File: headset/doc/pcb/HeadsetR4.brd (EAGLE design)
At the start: 85 x 56 mm, 58 parts, among them U1 STM32F405RGT6, U2 MAX17043, U3 MCP73831, U4 MIC5219, U5 MIC5219, U6 MIC5219 3.3V, U7 XBEE, U8 STEVAL-MKI108V2, Y1 8MHz

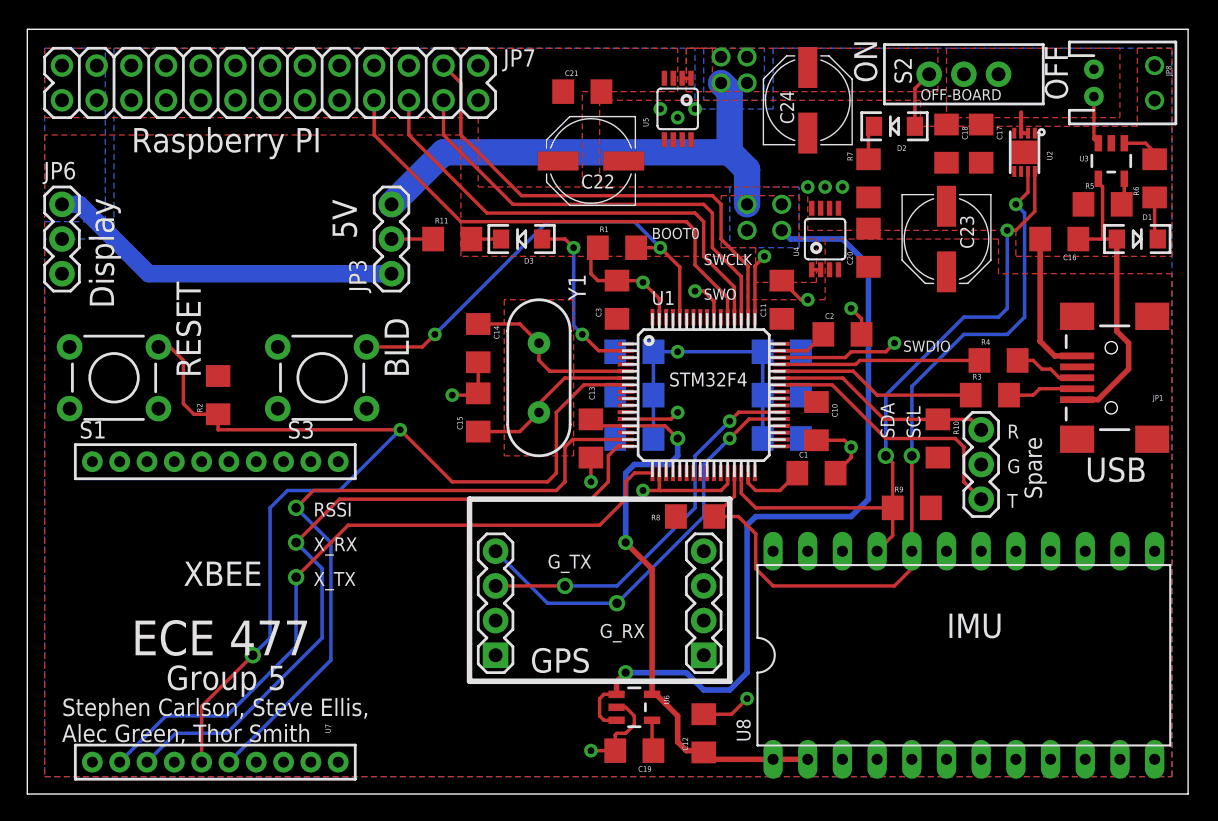
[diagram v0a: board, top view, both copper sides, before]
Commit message: Carlson updated pcb to add clearance on power planes.
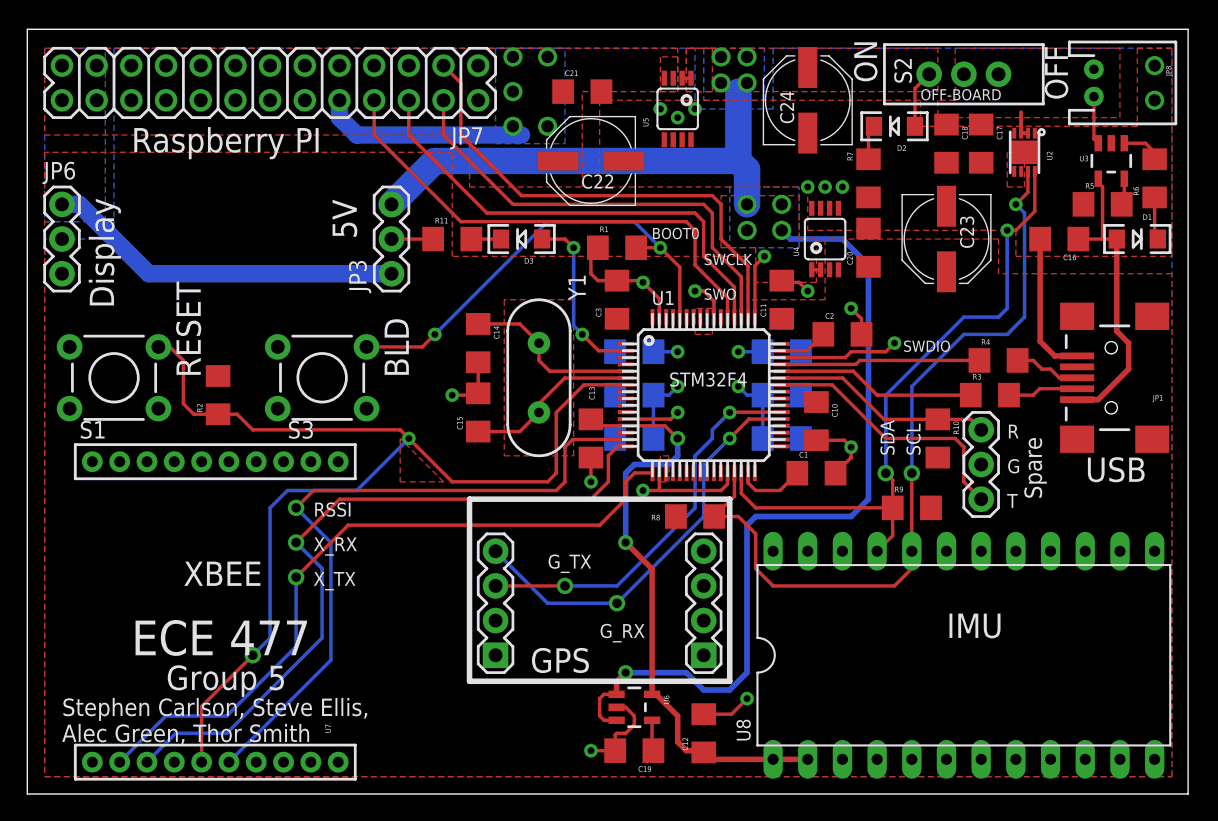
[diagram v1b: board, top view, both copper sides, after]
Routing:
- net V_CORE: track 0.00 -> 15.1 mm, vias 0 -> 5
- net V_MCU: track 20.7 -> 14.2 mm, vias 1 -> 4
- net V_IN: track 102.4 -> 101.6 mm
- added copper zone on layer 16, net V_CORE

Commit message: Carlson touched up pcb and schematic
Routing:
- net BC_STAT: track 3.01 -> 4.05 mm
- net X_RX: track 52.5 -> 52.0 mm
- net GND: vias 18 -> 20
- net BOOT0: vias 2 -> 1
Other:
- board text added: "!CS!"
- board text added: "5"
- board text added: "CHARGING"
- board text added: "GND"
- board text added: "MISO"
- board text added: "MOSI"
- board text added: "SCK"
- board text added: "STAT"
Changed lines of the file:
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@@
 <text x="2.54" y="3.81" size="1.27" layer="21">Stephen Carlson, Steve Ellis,
 Alec Green, Thor Smith</text>
-<text x="7.62" y="46.99" size="1.778" layer="21">Raspberry PI</text>
-<text x="6.35" y="35.56" size="1.778" layer="21" rot="R90">Display</text>
+<text x="5.715" y="46.99" size="1.778" layer="21">Raspberry PI</text>
+<text x="8.255" y="35.56" size="1.778" layer="21" rot="R90">Display</text>
 <text x="24.13" y="40.64" size="1.778" layer="21" rot="R90">5V</text>
 <text x="12.7" y="30.48" size="1.778" layer="21" rot="R90">RESET</text>
@@
 <text x="45.72" y="40.64" size="0.8128" layer="21">BOOT0</text>
 <text x="65.405" y="50.8" size="0.8128" layer="21">OFF-BOARD</text>
+<text x="18.415" y="20.32" size="1.016" layer="22" rot="MR0">RSSI</text>
+<text x="18.415" y="17.78" size="1.016" layer="22" rot="MR0">X_RX</text>
+<text x="18.415" y="15.24" size="1.016" layer="22" rot="MR0">X_TX</text>
+<text x="22.86" y="12.7" size="1.778" layer="22" rot="MR0">XBEE</text>
+<text x="40.64" y="12.7" size="1.016" layer="22" rot="MR0">G_TX</text>
+<text x="45.72" y="15.24" size="1.016" layer="22" rot="MR0">G_RX</text>
+<text x="71.12" y="11.43" size="1.778" layer="22" rot="MR0">IMU</text>
+<text x="78.74" y="29.21" size="1.778" layer="22" rot="MR0">USB</text>
+<text x="67.945" y="32.385" size="0.8128" layer="22" rot="MR0">SWDIO</text>
+<text x="53.34" y="38.735" size="0.8128" layer="22" rot="MR0">SWCLK</text>
+<text x="52.07" y="36.195" size="0.8128" layer="22" rot="MR0">SWO</text>
+<text x="49.53" y="40.64" size="0.8128" layer="22" rot="MR0">BOOT0</text>
+<text x="23.495" y="46.99" size="1.778" layer="22" rot="MR0">Raspberry PI</text>
+<text x="6.35" y="35.56" size="1.778" layer="22" rot="MR90">Display</text>
+<text x="22.86" y="40.64" size="1.778" layer="22" rot="MR90">5V</text>
+<text x="11.43" y="30.48" size="1.778" layer="22" rot="MR90">RESET</text>
+<text x="26.67" y="30.48" size="1.778" layer="22" rot="MR90">BLD</text>
+<text x="73.025" y="21.59" size="1.27" layer="22" rot="MR90">Spare</text>
+<text x="62.23" y="24.765" size="1.016" layer="22" rot="MR90">SDA</text>
+<text x="64.135" y="24.765" size="1.016" layer="22" rot="MR90">SCL</text>
+<text x="48.895" y="26.67" size="1.016" layer="22" rot="MR90">STM32F4</text>
+<text x="76.835" y="38.1" size="1.016" layer="21">CHARGING</text>
+<text x="64.135" y="46.355" size="1.016" layer="21">ON</text>
+<text x="34.29" y="37.465" size="1.016" layer="21">STAT</text>
+<text x="32.385" y="47.625" size="0.8128" layer="21" rot="R90">!CS!</text>
+<text x="31.115" y="46.99" size="0.8128" layer="21" rot="R90">SCK</text>
+<text x="28.575" y="46.355" size="0.8128" layer="21" rot="R90">MISO</text>
+<text x="26.035" y="46.355" size="0.8128" layer="21" rot="R90">MOSI</text>
+<text x="33.655" y="46.99" size="0.8128" layer="21" rot="R90">GND</text>
+<text x="4.445" y="37.465" size="1.016" layer="21">G</text>
+<text x="4.445" y="42.545" size="1.016" layer="21">5</text>
+<text x="5.08" y="42.545" size="1.016" layer="22" rot="MR0">5</text>
+<text x="5.08" y="37.465" size="1.016" layer="22" rot="MR0">G</text>
+<text x="72.39" y="26.035" size="1.016" layer="22" rot="MR0">R</text>
+<text x="72.39" y="23.495" size="1.016" layer="22" rot="MR0">G</text>
+<text x="72.39" y="20.955" size="1.016" layer="22" rot="MR0">T</text>
 </plain>
 <attributes>
@@
 <element name="C21" library="ECE477" package="1206" value="1u" x="40.64" y="51.435"/>
 <element name="U7" library="SparkFun-RF" package="XBEE-1" value="XBEE" x="24.765" y="13.335" rot="R90"/>
-<element name="D2" library="SparkFun-LED" package="LED-1206" value="PWR" x="63.5" y="48.895" rot="R180">
+<element name="D2" library="SparkFun-LED" package="LED-1206" value="PWR" x="63.5" y="48.895" smashed="yes" rot="R180">
 <attribute name="PROD_ID" value="DIO-00809" x="-13.97" y="130.175" size="1.778" layer="27" rot="R180" display="off"/>
+<attribute name="NAME" x="62.484" y="50.673" size="0.4064" layer="25" rot="R180"/>
+<attribute name="VALUE" x="64.516" y="50.673" size="0.4064" layer="27" rot="R180"/>
 </element>
 <element name="R7" library="ECE477" package="1206" value="470" x="61.595" y="45.085" smashed="yes" rot="R90">
@@
 </element>
 <element name="JP7" library="SparkFun-Connectors" package="2X13" value="R_PI" x="2.54" y="50.8" smashed="yes">
-<attribute name="NAME" x="31.0388" y="47.5488" size="1.27" layer="25" ratio="10"/>
+<attribute name="NAME" x="1.1938" y="47.5488" size="1.27" layer="25" ratio="10"/>
 <attribute name="VALUE" x="1.27" y="47.625" size="1.27" layer="27"/>
 </element>
@@
 <vertex x="30.48" y="22.86"/>
 </polygon>
+<via x="72.39" y="46.99" extent="1-16" drill="0.5"/>
+<via x="73.66" y="46.99" extent="1-16" drill="0.5"/>
 </signal>
 <signal name="VCAP2">
@@
 <wire x1="44.58" y1="40.005" x2="46.355" y2="40.005" width="0.254" layer="1"/>
 <via x="46.355" y="40.005" extent="1-16" drill="0.5"/>
-<wire x1="29.845" y1="33.655" x2="38.1" y2="41.91" width="0.254" layer="16"/>
+<wire x1="28.9306" y1="32.7406" x2="38.1" y2="41.91" width="0.254" layer="16"/>
 <wire x1="38.1" y1="41.91" x2="44.45" y2="41.91" width="0.254" layer="16"/>
 <wire x1="44.45" y1="41.91" x2="46.355" y2="40.005" width="0.254" layer="16"/>
-<via x="29.845" y="33.655" extent="1-16" drill="0.5"/>
-<wire x1="24.8412" y1="32.7406" x2="28.9306" y2="32.7406" width="0.254" layer="1"/>
-<wire x1="28.9306" y1="32.7406" x2="29.845" y2="33.655" width="0.254" layer="1"/>
+<wire x1="24.8412" y1="32.7406" x2="28.9306" y2="32.7406" width="0.254" layer="16"/>
 </signal>
 <signal name="OSC_IN">
@@
 <contactref element="C16" pad="1"/>
 <contactref element="D1" pad="A"/>
-<wire x1="78.425" y1="45.0549" x2="78.425" y2="44.765" width="0.254" layer="1"/>
-<wire x1="78.425" y1="44.765" x2="78.74" y2="44.45" width="0.254" layer="1"/>
-<wire x1="78.74" y1="44.45" x2="78.74" y2="40.64" width="0.254" layer="1"/>
-<wire x1="76.965" y1="40.64" x2="78.74" y2="40.64" width="0.254" layer="1"/>
-<wire x1="78.74" y1="40.64" x2="79.78" y2="40.64" width="0.254" layer="1"/>
+<wire x1="78.425" y1="45.0549" x2="78.425" y2="44.765" width="0.4064" layer="1"/>
+<wire x1="78.425" y1="44.765" x2="78.74" y2="44.45" width="0.4064" layer="1"/>
+<wire x1="78.74" y1="44.45" x2="78.74" y2="40.64" width="0.4064" layer="1"/>
+<wire x1="76.965" y1="40.64" x2="78.74" y2="40.64" width="0.4064" layer="1"/>
+<wire x1="78.74" y1="40.64" x2="79.78" y2="40.64" width="0.4064" layer="1"/>
 <wire x1="76.875" y1="28.88" x2="78.41" y2="28.88" width="0.4064" layer="1"/>
 <wire x1="78.41" y1="28.88" x2="80.645" y2="31.115" width="0.4064" layer="1"/>
@@
 <contactref element="JP1" pad="D+"/>
 <contactref element="R4" pad="2"/>
-<wire x1="76.875" y1="30.48" x2="75.565" y2="30.48" width="0.254" layer="1"/>
-<wire x1="75.565" y1="30.48" x2="74.93" y2="31.115" width="0.254" layer="1"/>
-<wire x1="74.93" y1="31.115" x2="74.295" y2="31.115" width="0.254" layer="1"/>
-<wire x1="74.295" y1="31.115" x2="73.66" y2="31.75" width="0.254" layer="1"/>
+<wire x1="76.875" y1="30.48" x2="74.93" y2="30.48" width="0.254" layer="1"/>
+<wire x1="74.93" y1="30.48" x2="73.66" y2="31.75" width="0.254" layer="1"/>
 <wire x1="73.66" y1="31.75" x2="72.52" y2="31.75" width="0.254" layer="1"/>
 </signal>
@@
 <polygon width="0.254" layer="1" isolate="0.3048" thermals="no">
 <vertex x="67.945" y="54.61"/>
-<vertex x="67.945" y="50.8"/>
+<vertex x="67.945" y="52.07"/>
 <vertex x="66.675" y="50.8"/>
 <vertex x="66.675" y="49.53"/>
@@
 <vertex x="80.01" y="54.61"/>
 </polygon>
-<wire x1="78.105" y1="51.07" x2="78.105" y2="47.9751" width="0.254" layer="1"/>
-<wire x1="78.105" y1="47.9751" x2="78.425" y2="47.6551" width="0.254" layer="1"/>
+<wire x1="78.105" y1="51.07" x2="78.105" y2="47.9751" width="0.4064" layer="1"/>
+<wire x1="78.105" y1="47.9751" x2="78.425" y2="47.6551" width="0.4064" layer="1"/>
 <wire x1="73.275" y1="48.39" x2="72.775" y2="48.39" width="0.3048" layer="1"/>
 <wire x1="72.775" y1="48.39" x2="72.775" y2="49.915" width="0.3048" layer="1"/>
@@
 <contactref element="R6" pad="2"/>
 <contactref element="U3" pad="1"/>
-<wire x1="80.325" y1="47.6551" x2="81.8849" y2="47.6551" width="0.254" layer="1"/>
-<wire x1="81.8849" y1="47.6551" x2="82.55" y2="46.99" width="0.254" layer="1"/>
-<wire x1="82.55" y1="46.99" x2="82.55" y2="46.485" width="0.254" layer="1"/>
+<wire x1="80.325" y1="47.6551" x2="80.325" y2="47.94" width="0.254" layer="1"/>
+<wire x1="80.325" y1="47.94" x2="80.645" y2="48.26" width="0.254" layer="1"/>
+<wire x1="80.645" y1="48.26" x2="81.915" y2="48.26" width="0.254" layer="1"/>
+<wire x1="81.915" y1="48.26" x2="82.55" y2="47.625" width="0.254" layer="1"/>
+<wire x1="82.55" y1="47.625" x2="82.55" y2="46.485" width="0.254" layer="1"/>
 </signal>
 <signal name="BC_STAT_LED">
@@
 <vertex x="48.26" y="54.61"/>
 <vertex x="48.26" y="51.435"/>
-<vertex x="66.675" y="51.435"/>
+<vertex x="66.04" y="51.435"/>
+<vertex x="66.04" y="52.07"/>
+<vertex x="66.675" y="52.07"/>
 <vertex x="66.675" y="54.61"/>
 </polygon>
@@
 <vertex x="48.26" y="54.61"/>
 <vertex x="48.26" y="51.435"/>
-<vertex x="50.165" y="51.435"/>
-<vertex x="50.165" y="54.61"/>
+<vertex x="58.42" y="51.435"/>
+<vertex x="58.42" y="54.61"/>
 </polygon>
 <wire x1="47.95" y1="52.415" x2="48.6" y2="52.415" width="0.254" layer="1"/>
@@
 <via x="19.685" y="18.415" extent="1-16" drill="0.7"/>
 <wire x1="22.86" y1="21.59" x2="19.685" y2="18.415" width="0.254" layer="1"/>
-<wire x1="19.685" y1="18.415" x2="21.59" y2="16.51" width="0.254" layer="16"/>
-<wire x1="21.59" y1="16.51" x2="21.59" y2="11.43" width="0.254" layer="16"/>
-<wire x1="21.59" y1="11.43" x2="14.605" y2="4.445" width="0.254" layer="16"/>
+<wire x1="19.685" y1="18.415" x2="20.955" y2="17.145" width="0.254" layer="16"/>
+<wire x1="20.955" y1="17.145" x2="20.955" y2="10.795" width="0.254" layer="16"/>
+<wire x1="20.955" y1="10.795" x2="14.605" y2="4.445" width="0.254" layer="16"/>
 <wire x1="14.605" y1="4.445" x2="10.875" y2="4.445" width="0.254" layer="16"/>
 <wire x1="10.875" y1="4.445" x2="8.765" y2="2.335" width="0.254" layer="16"/>
